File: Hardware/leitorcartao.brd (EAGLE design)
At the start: 34.5 x 56.7 mm, 166 parts, among them IC1 TL084, IC2 TL084, Q1 DMN3404, Q2 MMBT4401, Q3 MMBT4403, Q4 MMBT4401, Q5 MMBT4401, Q6 MMBT4401, Q7 MMBT4401, U1 LP2985-33DBVR, U2 TLV1117-50CDCYR, U3 SAMD20E14A-AUT, U4 MFRC52202HN1, X1 ANTENA, X2 MIFARE

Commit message: Mudanças nos PN dos reguladores de tensão.
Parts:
- U1: value LP2985-33DBVR -> TLV71333PDBVR
- U2: value TLV1117-50CDCYR -> NCP1117LPST50T3G

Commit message: BOM do protótipo v3 e início da alteração do layout para os novos parafusos.
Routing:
- net +12V: track 118.0 -> 103.7 mm

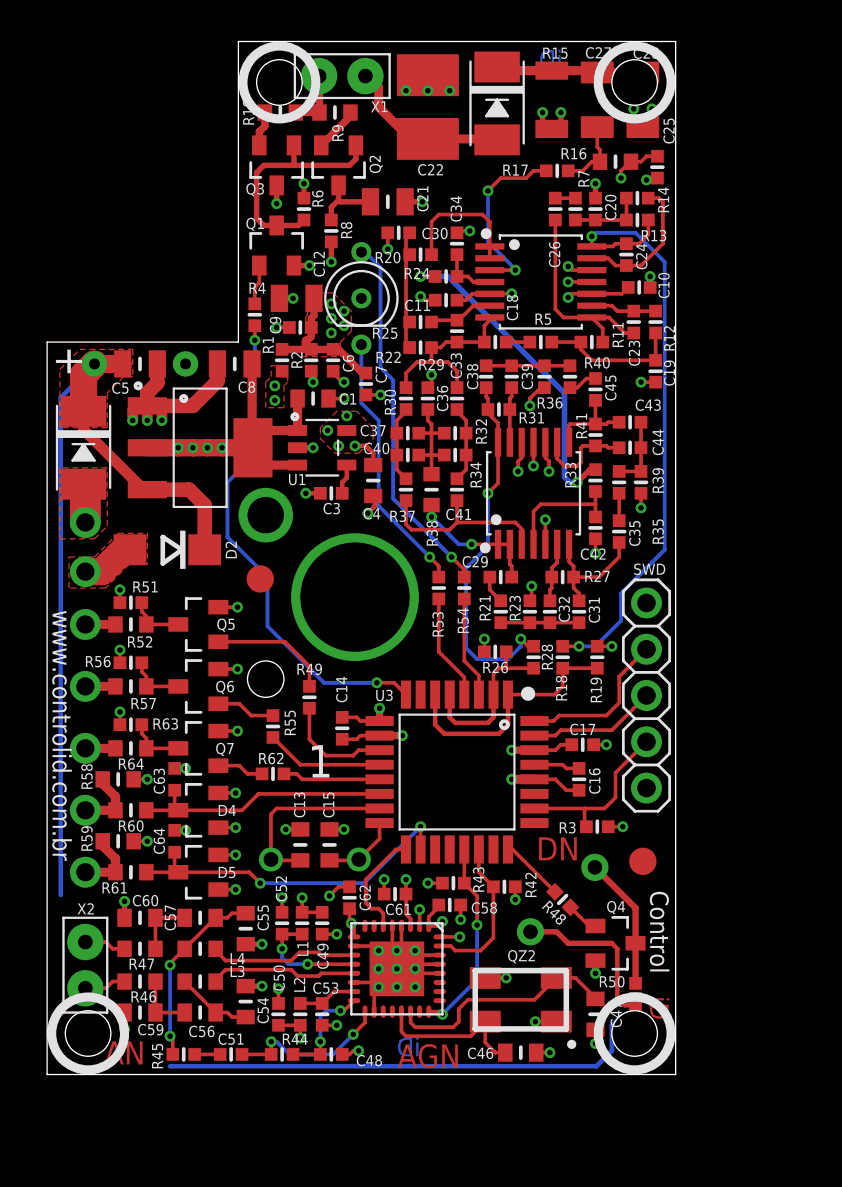
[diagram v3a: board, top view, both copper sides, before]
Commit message: Primeira solução para o posicionamento dos componentes e furos corrigidos.
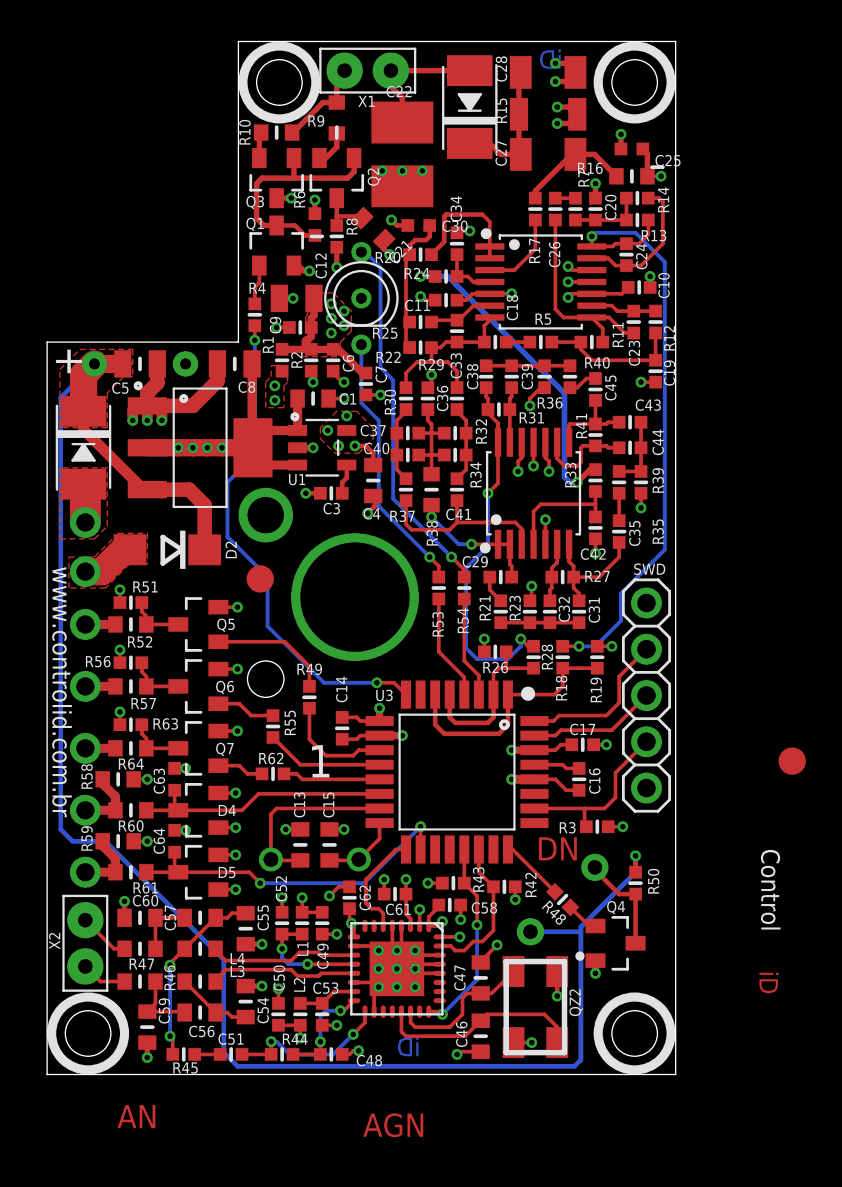
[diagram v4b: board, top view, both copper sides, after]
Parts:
- C21: device RFiD:C0805 -> RFiD:C0603
- moved FID3 9.87 mm to (40.9, 17.2)
- moved C47 6.61 mm to (23.8, 5.30), turned to 90 degrees
- moved R50 6.10 mm to (32.3, 10.5), turned to 90 degrees
- moved C28 5.41 mm to (27.5, 55.0), turned to 0 degrees
- moved C27 4.04 mm to (27.5, 50.5), turned to 0 degrees
- moved C22 2.95 mm to (19.5, 50.5), turned to 270 degrees
- moved R17 2.42 mm to (26.8, 47.5), turned to 90 degrees
- moved C46 2.38 mm to (23.8, 2.10), turned to 270 degrees
- moved C25 1.72 mm to (32.1, 50.8), turned to 180 degrees
- moved C21 1.70 mm to (17.9, 46.4), turned to 315 degrees
- moved D3 1.51 mm to (23.2, 53.1), turned to 90 degrees
- moved X1 1.43 mm to (17.6, 55.1)
- moved R16 1.20 mm to (32.1, 49.3)
- moved X2 1.20 mm to (2.10, 7.20)
- moved C30 1.17 mm to (20.4, 46.6)
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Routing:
- net +12V: track 103.7 -> 116.2 mm
- net N$58: track 10.0 -> 4.58 mm, vias 2 -> 0
- net N$5: track 12.9 -> 8.41 mm
- net N$3: track 8.61 -> 11.4 mm
- net N$14: track 3.92 -> 6.18 mm
- net N$9: track 9.32 -> 7.44 mm
- net N$11: track 3.31 -> 5.06 mm
- net N$54: track 7.29 -> 5.62 mm
- net GND: track 87.7 -> 89.1 mm
- net N$12: track 6.80 -> 7.84 mm
- net N$48: track 3.86 -> 3.14 mm
- net N$13: track 8.24 -> 7.63 mm
- net N$35: track 3.30 -> 3.91 mm
- net N$16: track 2.46 -> 1.95 mm

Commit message: Nova solução de posicionamento dos compoentes no leitor.
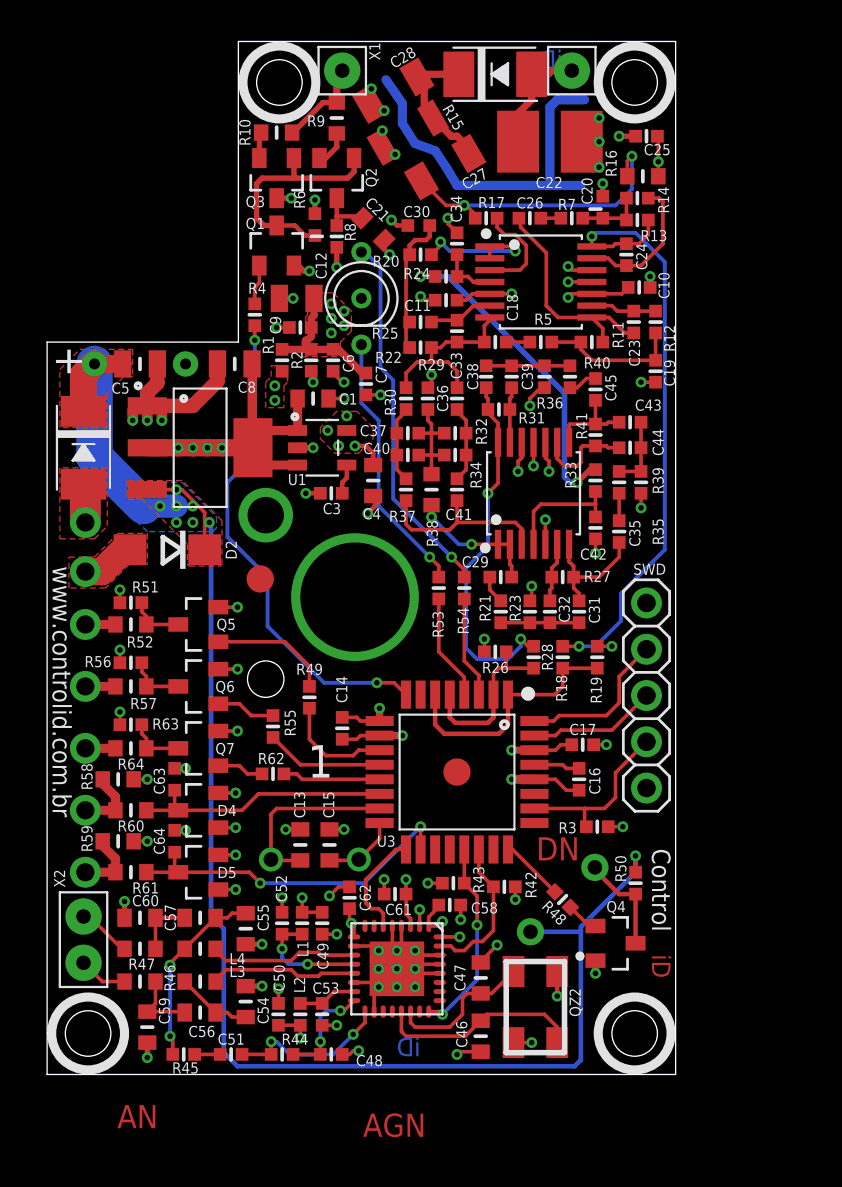
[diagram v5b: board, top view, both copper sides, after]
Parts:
- X2: device RFiD:22-23-2021 -> RFiD:ANTENNA
- moved FID3 18.4 mm to (22.5, 16.6)
- moved C28 8.56 mm to (19.0, 54.0), turned to 210 degrees
- moved C22 8.13 mm to (27.6, 51.2), turned to 0 degrees
- moved R15 7.76 mm to (19.8, 51.7), turned to 30 degrees
- moved C27 5.69 mm to (21.9, 49.8), turned to 210 degrees
- moved X1 4.90 mm to (22.5, 55.1)
- moved R17 2.75 mm to (24.1, 47.0), turned to 180 degrees
- moved D3 2.28 mm to (24.6, 54.9), turned to 0 degrees
- moved C26 1.49 mm to (26.5, 47.0), turned to 0 degrees
- moved C25 1.06 mm to (32.9, 51.5)
- moved R16 0.60 mm to (32.7, 49.3)
- moved R7 0.54 mm to (28.8, 47.0), turned to 0 degrees
- moved C20 0.41 mm to (30.5, 47.6)
- moved X2 0.22 mm to (2.00, 7.40)
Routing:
- net N$70: track 0.00 -> 20.6 mm
- net N$14: track 6.18 -> 16.5 mm, vias 0 -> 2
- net +12V: track 116.2 -> 107.1 mm, vias 7 -> 14
- net N$9: track 7.44 -> 6.29 mm
- net N$58: track 4.58 -> 5.66 mm
- net N$56: track 11.3 -> 12.4 mm
- net GND: track 89.1 -> 88.3 mm
- net N$10: track 7.10 -> 7.37 mm, vias 0 -> 2
- added copper zone on layer 16, net +12V

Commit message: Novas ideias para aumentar a isolação de alta tensão.
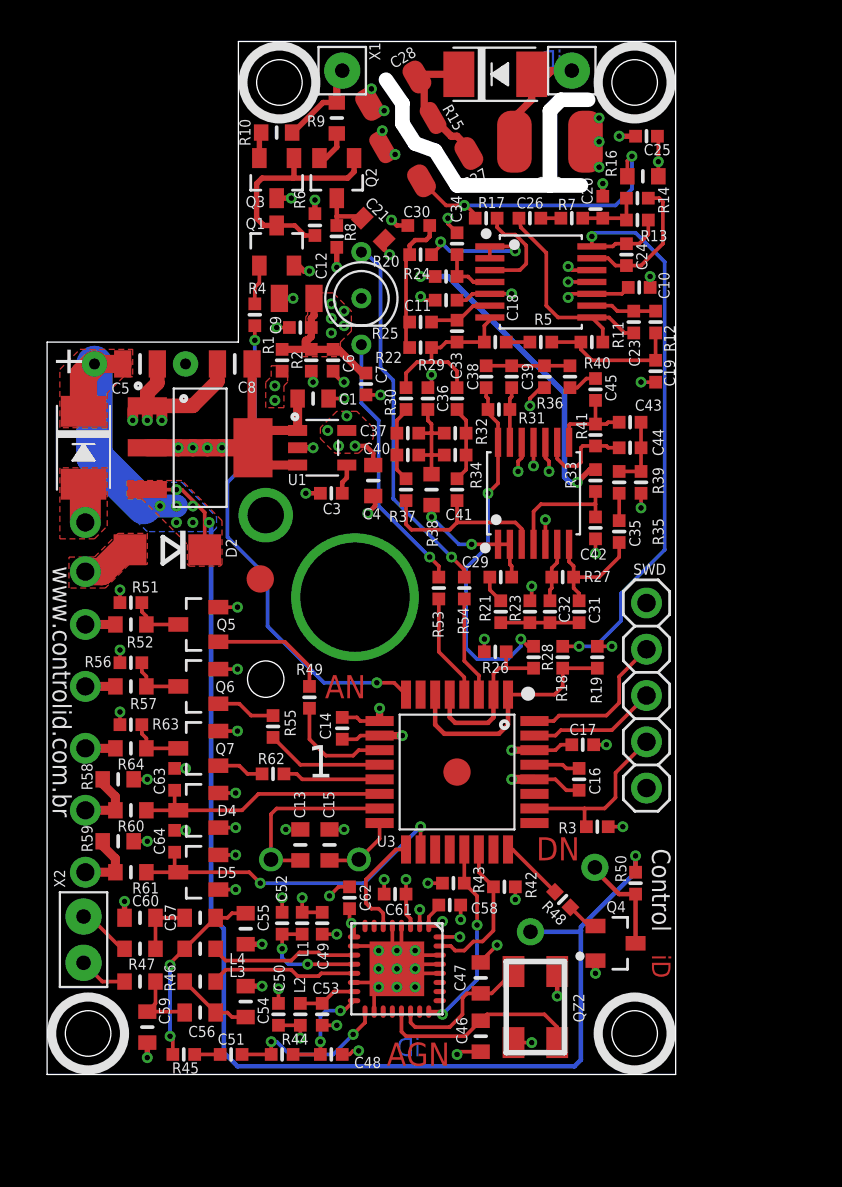
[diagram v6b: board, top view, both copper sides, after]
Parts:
- C22: device RFiD:C1812 -> RFiD:C1812S
- C27, C28: device RFiD:C1206 -> RFiD:C1206S
- R15: device RFiD:R1206 -> RFiD:R1206S
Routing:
- net N$70: track 20.6 -> 19.2 mm
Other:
- outline, holes or cut-outs redrawn

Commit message: Ajustes no silk das placas.
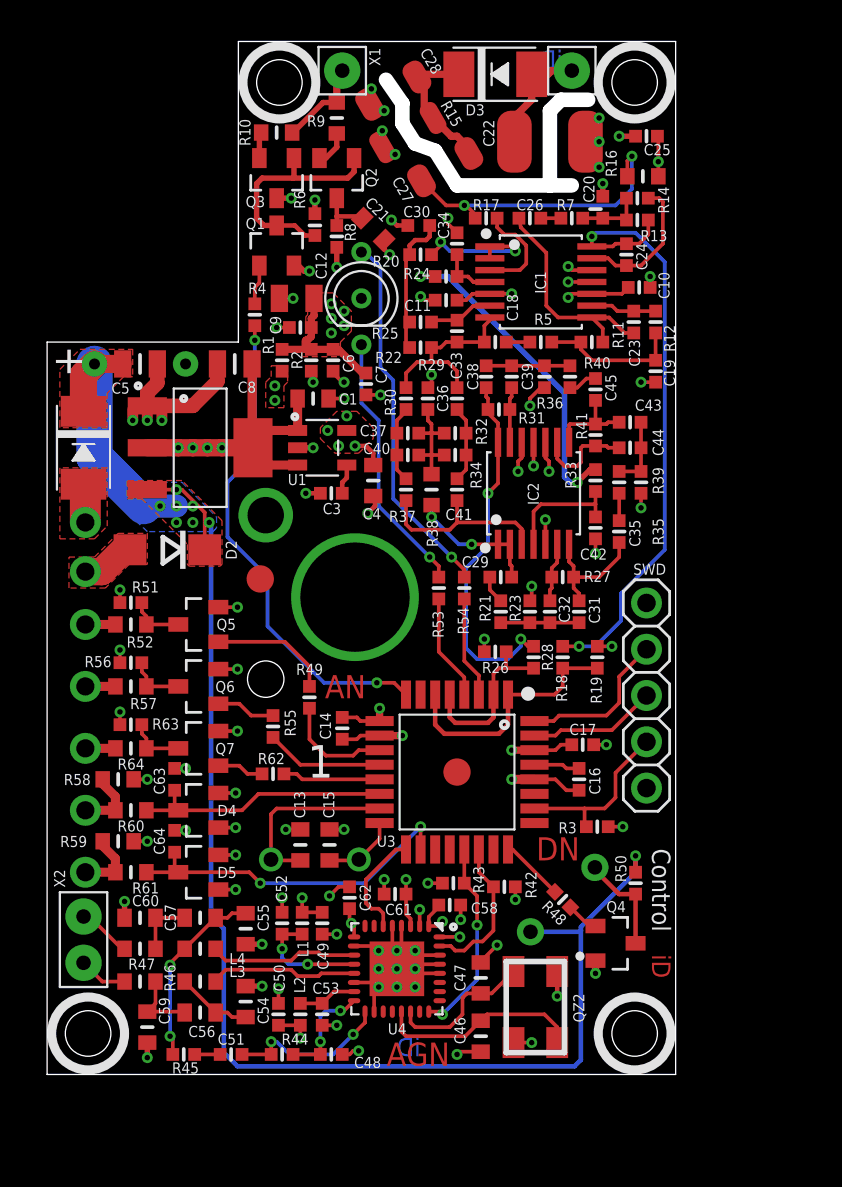
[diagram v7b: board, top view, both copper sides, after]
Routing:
- net N$70: track 19.2 -> 0.00 mm
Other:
- outline, holes or cut-outs redrawn

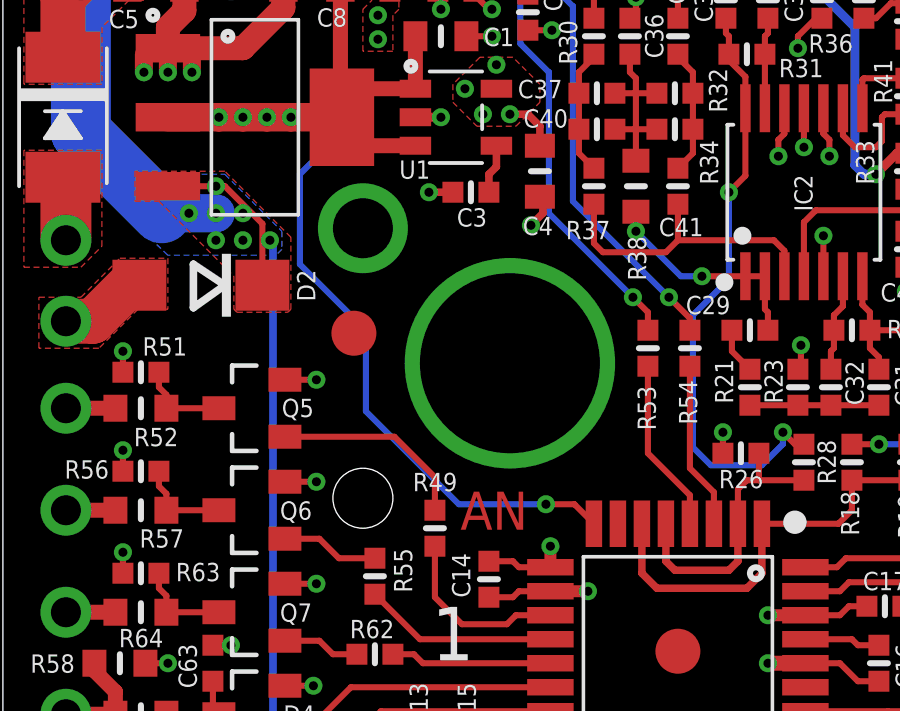
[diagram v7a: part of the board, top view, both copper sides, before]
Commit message: Aumento nos furos de cinta plástica e do furo do cabo.
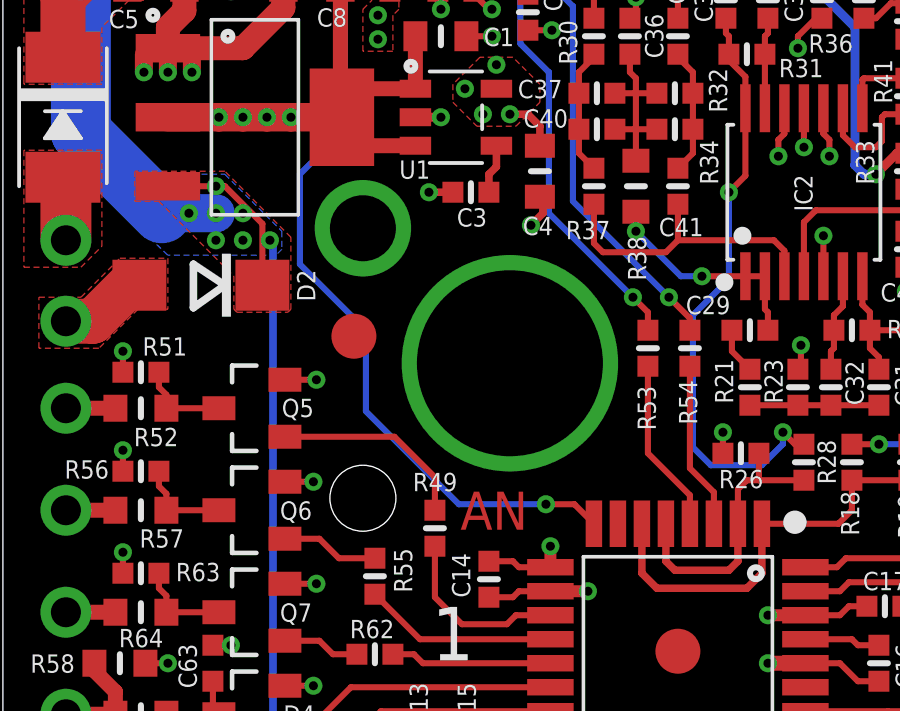
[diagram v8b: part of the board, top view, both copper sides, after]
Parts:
- moved FID1 0.10 mm to (11.7, 27.1)
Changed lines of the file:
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@@
 <layer number="22" name="bPlace" color="7" fill="1" visible="no" active="yes"/>
 <layer number="23" name="tOrigins" color="15" fill="1" visible="yes" active="yes"/>
-<layer number="24" name="bOrigins" color="15" fill="1" visible="yes" active="yes"/>
+<layer number="24" name="bOrigins" color="15" fill="1" visible="no" active="yes"/>
 <layer number="25" name="tNames" color="7" fill="1" visible="yes" active="yes"/>
 <layer number="26" name="bNames" color="7" fill="1" visible="no" active="yes"/>
@@
 <layer number="42" name="bRestrict" color="1" fill="10" visible="no" active="yes"/>
 <layer number="43" name="vRestrict" color="2" fill="10" visible="no" active="yes"/>
-<layer number="44" name="Drills" color="7" fill="1" visible="no" active="yes"/>
+<layer number="44" name="Drills" color="7" fill="1" visible="yes" active="yes"/>
 <layer number="45" name="Holes" color="7" fill="1" visible="yes" active="yes"/>
-<layer number="46" name="Milling" color="3" fill="1" visible="yes" active="yes"/>
+<layer number="46" name="Milling" color="3" fill="1" visible="no" active="yes"/>
 <layer number="47" name="Measures" color="7" fill="1" visible="yes" active="yes"/>
 <layer number="48" name="Document" color="7" fill="1" visible="yes" active="yes"/>
@@
 <wire x1="0" y1="40.2" x2="10.5" y2="40.2" width="0" layer="20"/>
 <wire x1="10.5" y1="40.2" x2="10.5" y2="56.7" width="0" layer="20"/>
-<hole x="12" y="21.7" drill="2"/>
+<hole x="12" y="21.7" drill="2.2"/>
 <text x="18.1" y="12.5" size="0.6096" layer="21" font="vector" ratio="11">U3</text>
 <text x="28.85" y="19.75" size="0.6096" layer="22" font="vector" ratio="11" rot="MR0">!RESET</text>
@@
 <attribute name="SPECIAL" value="" x="15.6" y="31.9" size="1.778" layer="27" rot="R180" display="off"/>
 </element>
-<element name="FID1" library="RFiD" package="FIDUCIAL-1.5X3" value="FIDUCIAL1.5X3" x="11.7" y="27.2">
-<attribute name="ASK" value="" x="11.7" y="27.2" size="1.778" layer="27" display="off"/>
-<attribute name="ASK_CUSTOMERPN" value="" x="11.7" y="27.2" size="1.778" layer="27" display="off"/>
-<attribute name="ASK_PN" value="" x="11.7" y="27.2" size="1.778" layer="27" display="off"/>
-<attribute name="CUSTOMERPN" value="" x="11.7" y="27.2" size="1.778" layer="27" display="off"/>
-<attribute name="FSK" value="" x="11.7" y="27.2" size="1.778" layer="27" display="off"/>
-<attribute name="FSK_CUSTOMERPN" value="" x="11.7" y="27.2" size="1.778" layer="27" display="off"/>
-<attribute name="FSK_PN" value="" x="11.7" y="27.2" size="1.778" layer="27" display="off"/>
-<attribute name="MIFARE" value="" x="11.7" y="27.2" size="1.778" layer="27" display="off"/>
-<attribute name="MIFARE_CUSTOMERPN" value="" x="11.7" y="27.2" size="1.778" layer="27" display="off"/>
-<attribute name="MIFARE_PN" value="" x="11.7" y="27.2" size="1.778" layer="27" display="off"/>
-<attribute name="PASSIVO" value="" x="11.7" y="27.2" size="1.778" layer="27" display="off"/>
-<attribute name="PN1" value="" x="11.7" y="27.2" size="1.778" layer="27" display="off"/>
-<attribute name="PSK" value="" x="11.7" y="27.2" size="1.778" layer="27" display="off"/>
-<attribute name="PSK_CUSTOMERPN" value="" x="11.7" y="27.2" size="1.778" layer="27" display="off"/>
-<attribute name="PSK_PN" value="" x="11.7" y="27.2" size="1.778" layer="27" display="off"/>
-<attribute name="SPECIAL" value="" x="11.7" y="27.2" size="1.778" layer="27" display="off"/>
+<element name="FID1" library="RFiD" package="FIDUCIAL-1.5X3" value="FIDUCIAL1.5X3" x="11.7" y="27.1">
+<attribute name="ASK" value="" x="11.7" y="27.1" size="1.778" layer="27" display="off"/>
+<attribute name="ASK_CUSTOMERPN" value="" x="11.7" y="27.1" size="1.778" layer="27" display="off"/>
+<attribute name="ASK_PN" value="" x="11.7" y="27.1" size="1.778" layer="27" display="off"/>
+<attribute name="CUSTOMERPN" value="" x="11.7" y="27.1" size="1.778" layer="27" display="off"/>
+<attribute name="FSK" value="" x="11.7" y="27.1" size="1.778" layer="27" display="off"/>
+<attribute name="FSK_CUSTOMERPN" value="" x="11.7" y="27.1" size="1.778" layer="27" display="off"/>
+<attribute name="FSK_PN" value="" x="11.7" y="27.1" size="1.778" layer="27" display="off"/>
+<attribute name="MIFARE" value="" x="11.7" y="27.1" size="1.778" layer="27" display="off"/>
+<attribute name="MIFARE_CUSTOMERPN" value="" x="11.7" y="27.1" size="1.778" layer="27" display="off"/>
+<attribute name="MIFARE_PN" value="" x="11.7" y="27.1" size="1.778" layer="27" display="off"/>
+<attribute name="PASSIVO" value="" x="11.7" y="27.1" size="1.778" layer="27" display="off"/>
+<attribute name="PN1" value="" x="11.7" y="27.1" size="1.778" layer="27" display="off"/>
+<attribute name="PSK" value="" x="11.7" y="27.1" size="1.778" layer="27" display="off"/>
+<attribute name="PSK_CUSTOMERPN" value="" x="11.7" y="27.1" size="1.778" layer="27" display="off"/>
+<attribute name="PSK_PN" value="" x="11.7" y="27.1" size="1.778" layer="27" display="off"/>
+<attribute name="SPECIAL" value="" x="11.7" y="27.1" size="1.778" layer="27" display="off"/>
 </element>
 <element name="FID3" library="RFiD" package="FIDUCIAL-1.5X3" value="FIDUCIAL1.5X3" x="22.5" y="16.6">
@@
 <contactref element="C20" pad="2"/>
 <contactref element="U1" pad="2"/>
-<via x="16.9" y="26.2" extent="1-16" drill="6"/>
-<via x="12" y="30.7" extent="1-16" drill="2" diameter="2"/>
+<via x="16.9" y="26.2" extent="1-16" drill="6.2"/>
+<via x="12" y="30.7" extent="1-16" drill="2.2" diameter="2"/>
 <contactref element="R2" pad="1"/>
 <contactref element="C6" pad="2"/>
@@
 <wire x1="9.4" y1="18.85" x2="10.45" y2="18.85" width="0.2032" layer="1"/>
 <via x="10.45" y="18.85" extent="1-16" drill="0.3"/>
-<wire x1="9.4" y1="22.25" x2="10.45" y2="22.25" width="0.2032" layer="1"/>
-<via x="10.45" y="22.25" extent="1-16" drill="0.3"/>
+<wire x1="9.4" y1="22.25" x2="10.35" y2="22.25" width="0.2032" layer="1"/>
+<via x="10.35" y="22.25" extent="1-16" drill="0.3"/>
 <wire x1="9.4" y1="25.65" x2="10.45" y2="25.65" width="0.2032" layer="1"/>
 <via x="10.45" y="25.65" extent="1-16" drill="0.3"/>
